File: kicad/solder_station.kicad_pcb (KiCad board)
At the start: 2 copper layers, 32 parts, among them IC1 OPA336U, P2 POWER, P3 MCU, P4 KEYPAD, P5 JACK, SW1 SPST, SW2 SPST, SW3 SPST, SW4 SPST, T1 IRF7476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

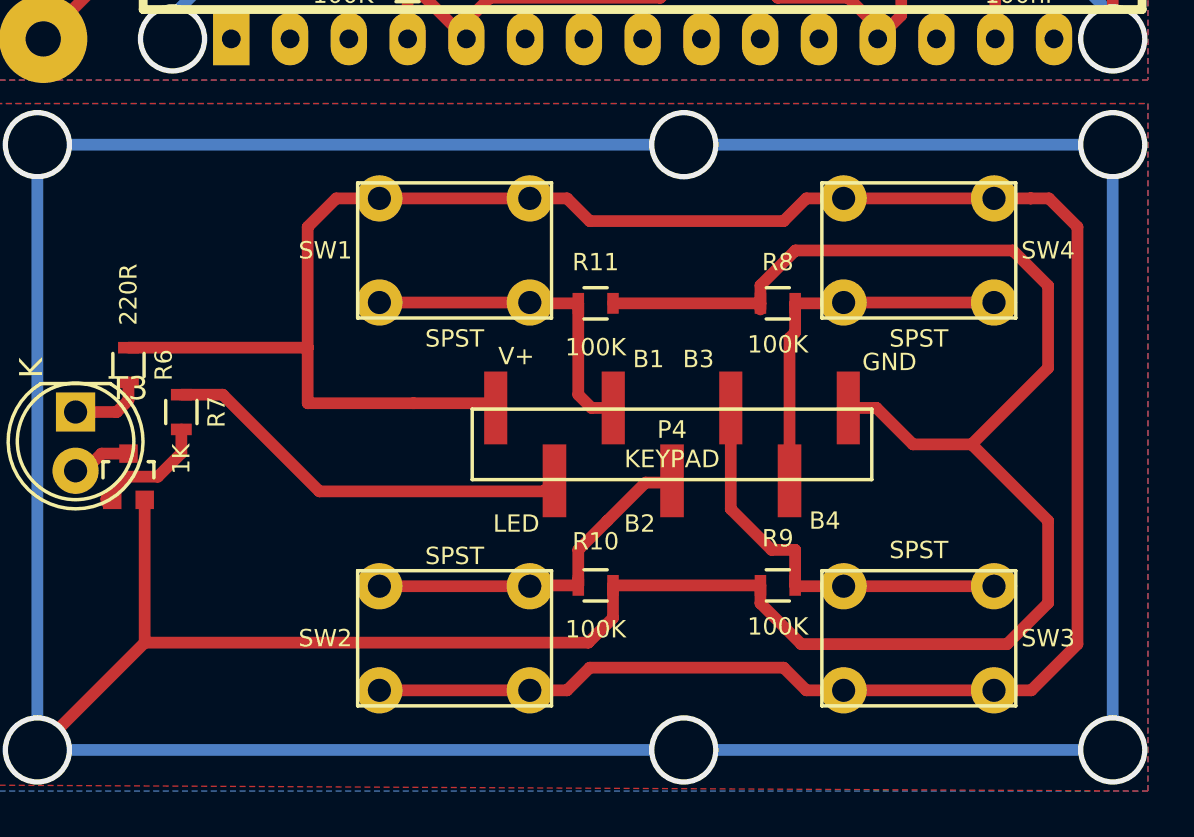
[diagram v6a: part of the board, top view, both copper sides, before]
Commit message: Add rotative encoder
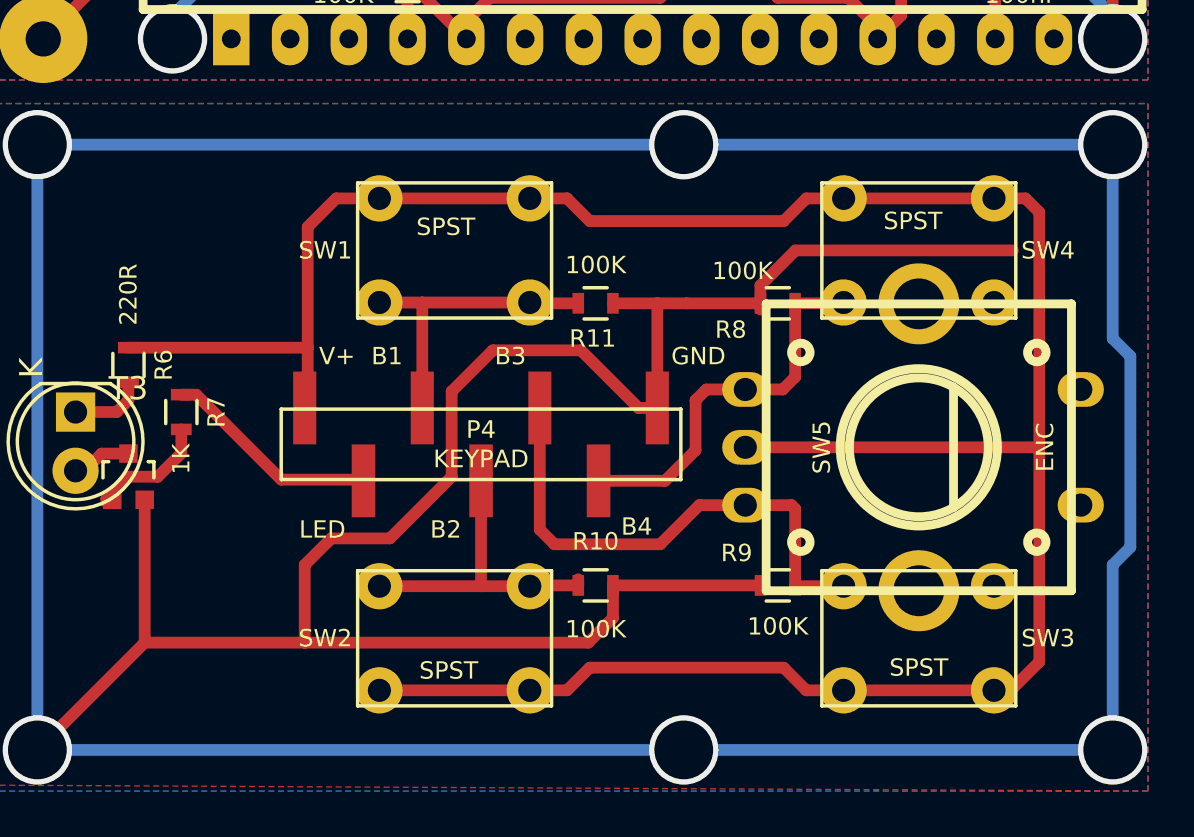
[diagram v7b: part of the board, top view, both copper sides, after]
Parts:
- added SW5: ENC, footprint:encoder_alps-ec12d, F.Cu at (164.1, 121.0)
- moved P4 8.25 mm to (145.2, 120.9)
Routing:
- net PIN_LED: track 18.0 -> 9.42 mm
- net PIN_GND: track 244.7 -> 236.2 mm
- net PIN_B3: track 18.0 -> 22.7 mm
- net PIN_B2: track 15.7 -> 13.4 mm
- net PIN_V+: track 108.6 -> 110.8 mm
- net PIN_B1: track 14.3 -> 13.2 mm
- net PIN_B4: track 16.4 -> 17.0 mm

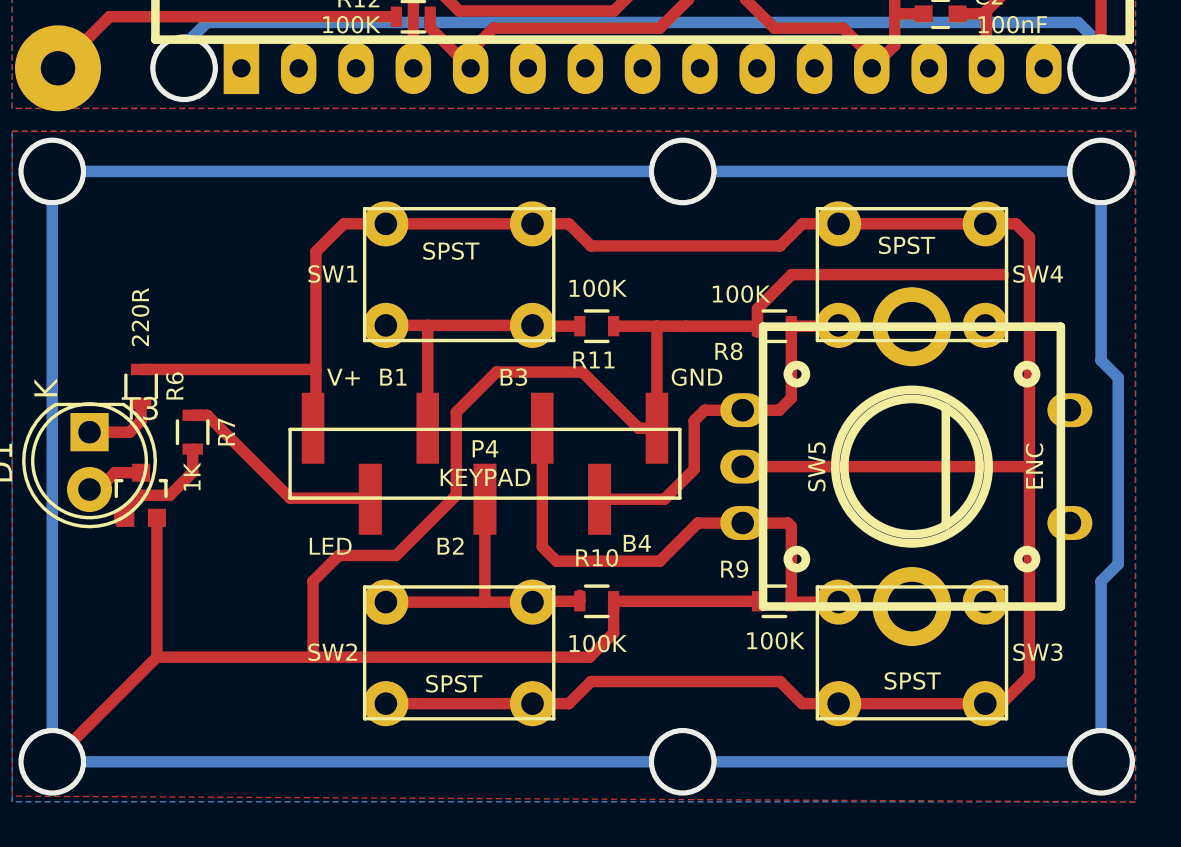
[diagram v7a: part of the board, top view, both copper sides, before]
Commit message: Use 12x12 mm button
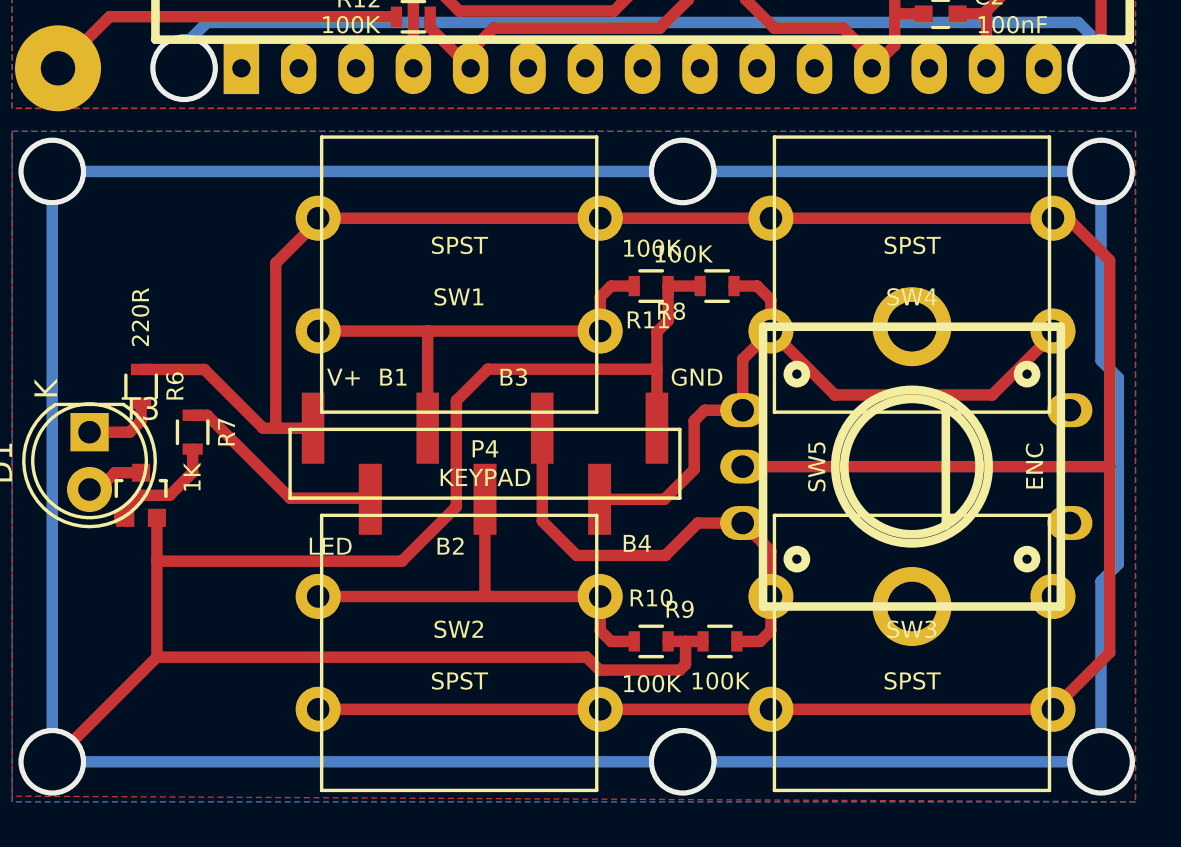
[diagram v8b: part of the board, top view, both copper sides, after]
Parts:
- SW1, SW2, SW3, SW4: footprint footprint:SW_65_45 -> footprint:SW_125_50
- moved R8 3.10 mm to (155.4, 113.0)
- moved R9 3.00 mm to (155.6, 128.8)
- moved R11 3.00 mm to (152.5, 113.0)
- moved R10 3.00 mm to (152.5, 128.8)
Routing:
- net PIN_GND: track 236.2 -> 221.3 mm
- net PIN_B4: track 17.0 -> 31.7 mm
- net PIN_V+: track 110.8 -> 124.6 mm
- net PIN_B1: track 13.2 -> 20.0 mm
- net PIN_B2: track 13.4 -> 20.0 mm
- net PIN_B3: track 22.7 -> 21.2 mm
